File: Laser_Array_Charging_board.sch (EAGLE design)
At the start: 22 parts, among them P1 12V/3V_DC/DC_CONVERTER, X1 6ESRM-P

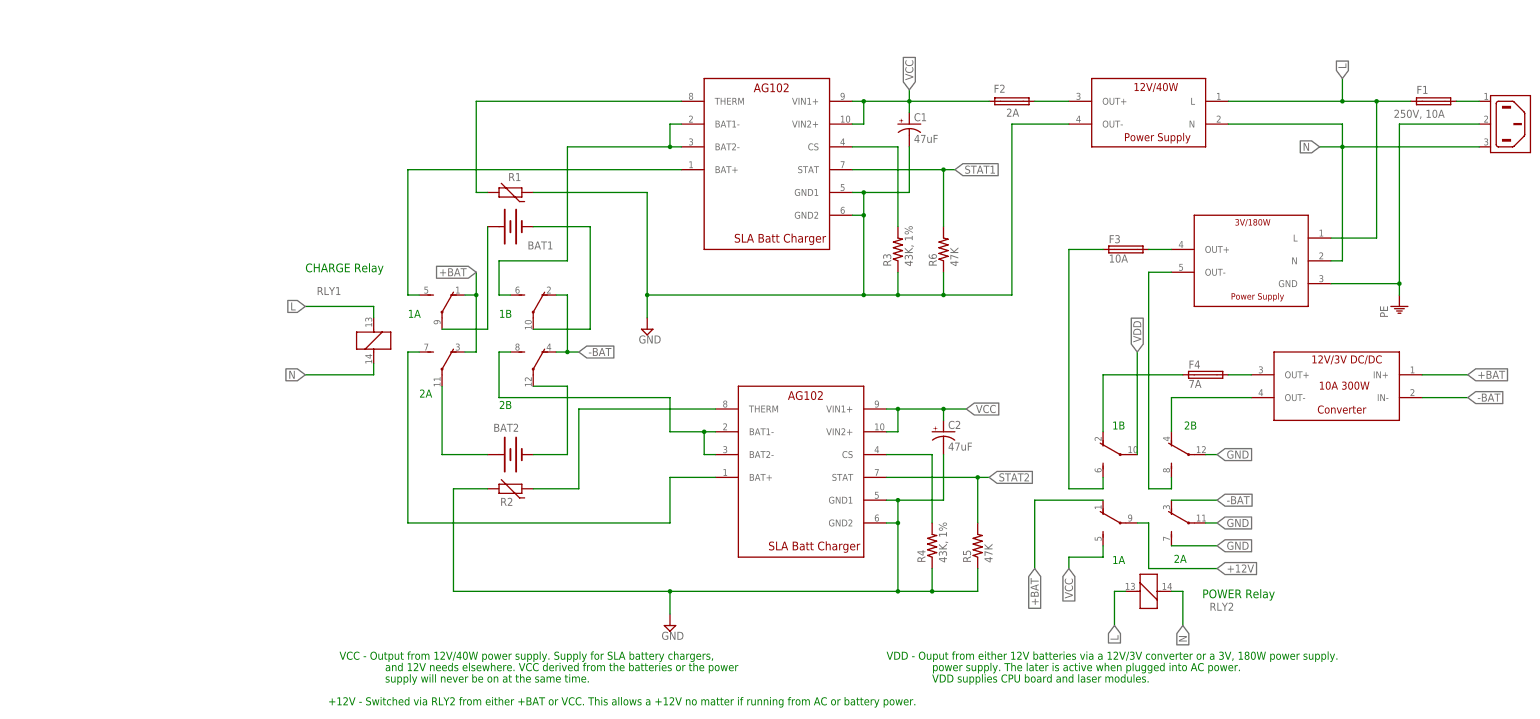
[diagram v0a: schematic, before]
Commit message: CPU board with headers moved over and with programming jack. V1.0
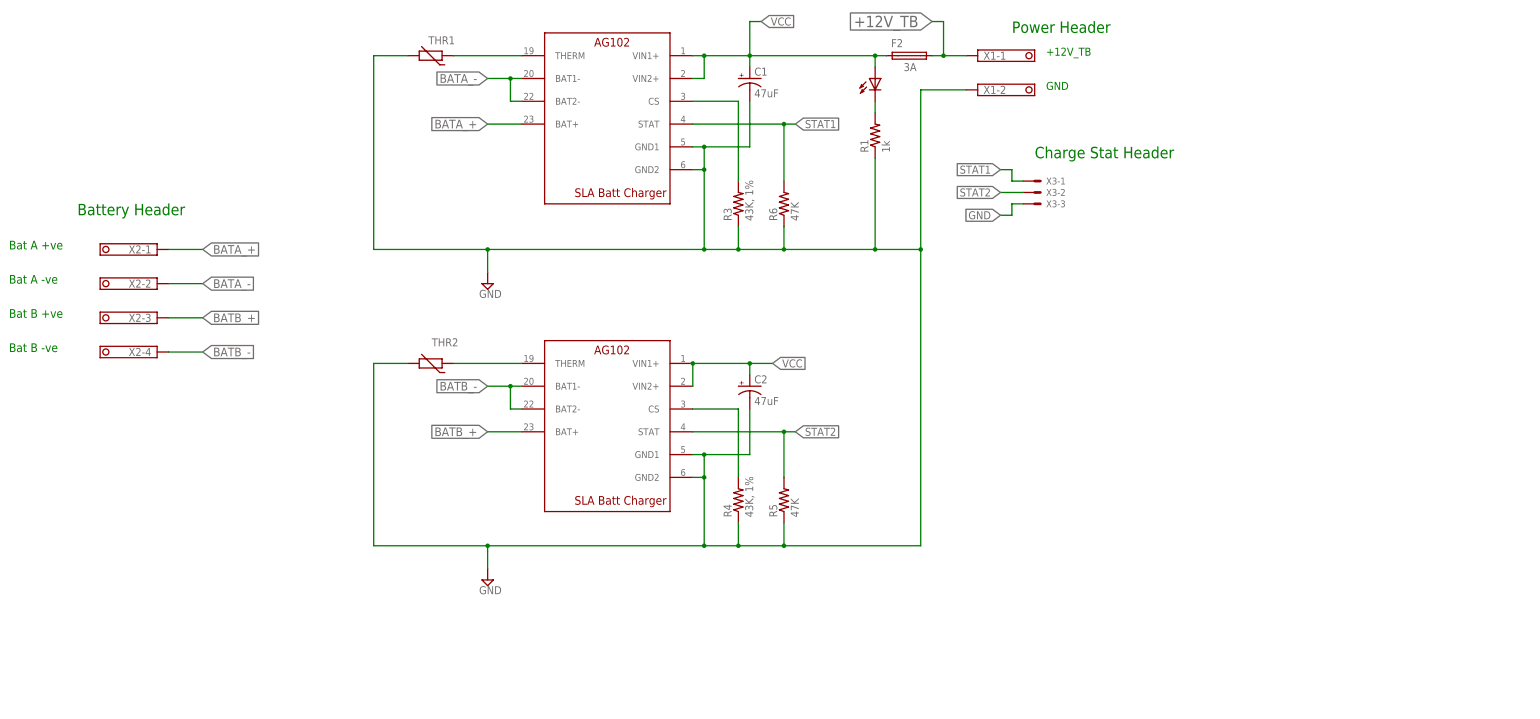
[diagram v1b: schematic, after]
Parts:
- removed BAT1, BAT2: (no value), Mine:BATTERY
- removed F1: 250V, 10A, fuse:SH22,5
- removed F3: 10A, fuse:SH22,5
- removed F4: 7A, fuse:SH22,5
- removed P1: 12V/3V_DC/DC_CONVERTER, Mine:12V/3V_DC/DC_CONVERTER
- removed PS1: 12V/40W_POWER_SUPPLY, Mine:12V/40W_POWER_SUPPLY
- removed PS2: 3V/180W_POWER_SUPPLY, Mine:3V/180W_POWER_SUPPLY
- removed R2: THERMISTOR-2,5, Mine:THERMISTOR-2,5
- removed RLY1, RLY2: 4P4T_RELAYS, Mine:4P4T_RELAYS
- added LED1: LEDCHIPLED_0805, Mine:LEDCHIPLED_0805
- added THR1, THR2: THERMISTOR-2,5, Mine:THERMISTOR-2,5
- added X2: 1751264, con-phoenix-350:1751264
- added X3: 22-23-2031, Mine:22-23-2031
- F2: value 2A -> 3A
- R1: value THERMISTOR-2,5 -> 1k; device Mine:THERMISTOR-2,5 -> rcl:R-US_M0805
- X1: value 6ESRM-P -> 1751248; device con-tycoelectronics:6ESRM-P -> con-phoenix-350:1751248
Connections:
- removed net +12V: RLY21.P
- removed net +BAT: P1.IN+, RLY11.O, RLY13.O, RLY21.O
- removed net -BAT: P1.IN-, RLY12.O, RLY14.O, RLY23.O
- removed net L: F1.1, PS1.L, PS2.L, RLY1_.1, RLY2_.1
- removed net N: PS1.N, PS2.N, RLY1_.2, RLY2_.2, X1.AC2
- removed net N$10: PS2.OUT-, RLY24.S
- removed net N$11: CHG1.BAT+, RLY11.S
- removed net N$12: CHG1.THERM, R1.2
- removed net N$14: CHG2.THERM, R2.1
- removed net N$15: CHG2.BAT1-, CHG2.BAT2-, RLY14.S
- removed net N$16: F1.2, X1.AC1
- removed net N$17: CHG2.BAT+, RLY13.S
- removed net N$18: F2.2, PS1.OUT+
- removed net N$19: F3.2, PS2.OUT+
- removed net N$20: F4.2, P1.OUT+
- removed net N$4: BAT1.-, RLY12.P
- removed net N$5: BAT2.+@1, RLY13.P
- removed net N$6: CHG1.BAT1-, CHG1.BAT2-, RLY12.S
- removed net N$8: BAT2.-, RLY14.P
- removed net N$9: F4.1, RLY22.O
- removed net PE: PS2.GND, X1.SH
- removed net VDD: RLY22.P
- new net +12V_TB: F2.2, X1-1.K
- new net BATA_+: CHG1.BAT+, X2-1.K
- new net BATA_-: CHG1.BAT1-, CHG1.BAT2-, X2-2.K
- new net BATB_+: CHG2.BAT+, X2-3.K
- new net BATB_-: CHG2.BAT1-, CHG2.BAT2-, X2-4.K
- net GND: now also THR1.2, THR2.2, X1-2.K, X3-3.S; no longer PS1.OUT-, R2.2, RLY23.P, RLY23.S, RLY24.P
- net N$1: now also CHG1.THERM, THR1.1; no longer P1.OUT-, RLY24.O
- net N$2: now also CHG2.THERM, THR2.1; no longer F3.1, RLY22.S
- net N$3: now also LED1.C, R1.2; no longer BAT1.+@1, RLY11.P
- net STAT1: now also X3-1.S
- net STAT2: now also X3-2.S
- net VCC: now also LED1.A; no longer RLY21.S
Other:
- note added: "+12V_TB"
- note added: "Bat A +ve"
- note added: "Bat A -ve"
- note added: "Bat B +ve"
- note added: "Bat B -ve"
- note added: "Battery Header"
- note added: "Charge Stat Header"
- note added: "GND"
- note added: "Power Header"
- note removed: "+12V - Switched via RLY2 from either +BAT or VCC. This allows a +12V no matter if running from AC or battery power."
- note removed: "1A"
- note removed: "1B"
- note removed: "2A"
- note removed: "2B"
- note removed: "CHARGE Relay"
- note removed: "POWER Relay"
- note removed: "VCC - Output from 12V/40W power supply. Supply for SLA battery chargers,"
- note removed: "VDD - Ouput from either 12V batteries via a 12V/3V converter or a 3V, 180W power supply."
- note removed: "VDD supplies CPU board and laser modules."
- note removed: "and 12V needs elsewhere. VCC derived from the batteries or the power"
- note removed: "power supply. The later is active when plugged into AC power."
- note removed: "supply will never be on at the same time."
- moved on the sheet: C1, C2, F2, R3, R4, R5, R6

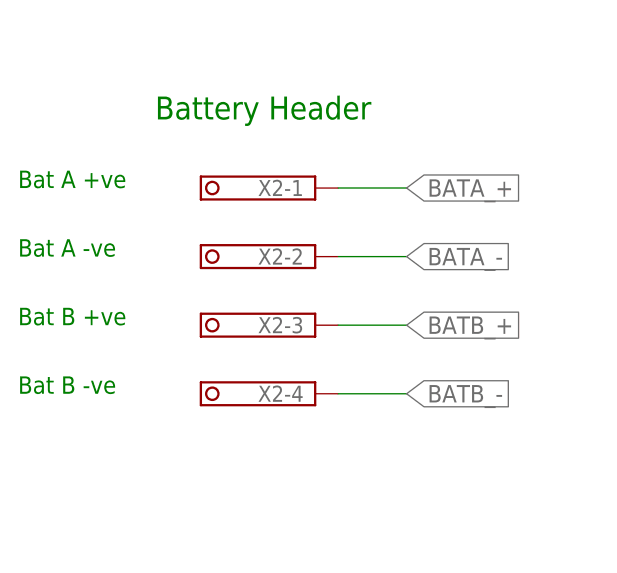
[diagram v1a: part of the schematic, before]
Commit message: Charging Board  header change, V1.1
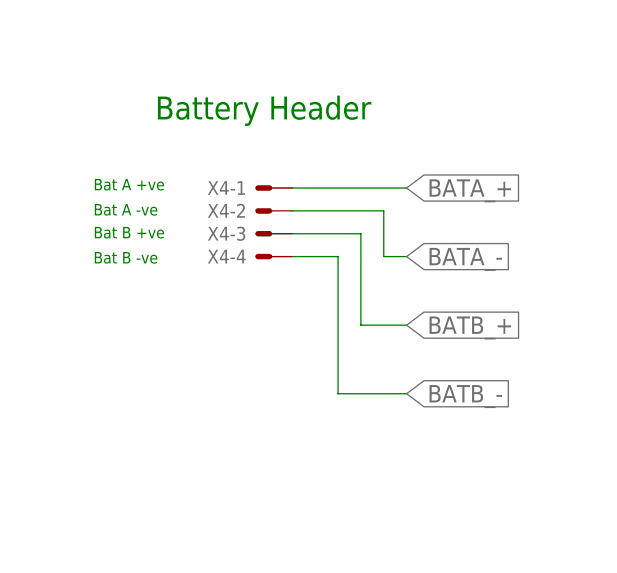
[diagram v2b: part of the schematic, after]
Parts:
- removed X2: 1751264, con-phoenix-350:1751264
- added X4: 22-23-2041, Mine:22-23-2041
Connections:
- net BATA_+: now also X4-1.S; no longer X2-1.K
- net BATA_-: now also X4-2.S; no longer X2-2.K
- net BATB_+: now also X4-3.S; no longer X2-3.K
- net BATB_-: now also X4-4.S; no longer X2-4.K
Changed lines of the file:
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@@
 <part name="F2" library="fuse" deviceset="SH22,5" device="" value="3A"/>
 <part name="CHG2" library="Mine" deviceset="AG102_SLA_CHARGER" device=""/>
-<part name="X2" library="con-phoenix-350" deviceset="1751264" device=""/>
 <part name="X1" library="con-phoenix-350" deviceset="1751248" device=""/>
 <part name="X3" library="Mine" deviceset="22-23-2031" device=""/>
@@
 <part name="LED1" library="Mine" deviceset="LED" device="CHIPLED_0805"/>
 <part name="R1" library="rcl" deviceset="R-US_" device="M0805" value="1k"/>
+<part name="X4" library="Mine" deviceset="22-23-2041" device=""/>
 </parts>
 <sheets>
@@
 <text x="76.2" y="68.58" size="1.778" layer="91">+12V_TB</text>
 <text x="76.2" y="60.96" size="1.778" layer="91">GND</text>
-<text x="-154.94" y="25.4" size="1.9304" layer="91">Bat A +ve</text>
-<text x="-154.94" y="17.78" size="1.9304" layer="91">Bat A -ve</text>
-<text x="-154.94" y="2.54" size="1.9304" layer="91">Bat B -ve</text>
-<text x="-154.94" y="10.16" size="1.9304" layer="91">Bat B +ve</text>
+<text x="-146.558" y="25.146" size="1.27" layer="91">Bat A +ve</text>
+<text x="-146.558" y="22.352" size="1.27" layer="91">Bat A -ve</text>
+<text x="-146.558" y="17.018" size="1.27" layer="91">Bat B -ve</text>
+<text x="-146.558" y="19.812" size="1.27" layer="91">Bat B +ve</text>
 <text x="-139.7" y="33.02" size="2.54" layer="91">Battery Header</text>
 <text x="68.58" y="73.66" size="2.54" layer="91">Power Header</text>
@@
 </instance>
 <instance part="CHG2" gate="G$1" x="-25.4" y="-10.16" rot="MR0"/>
-<instance part="X2" gate="-1" x="-121.92" y="25.4" smashed="yes" rot="MR0">
-<attribute name="NAME" x="-123.19" y="24.511" size="1.778" layer="95" rot="MR0"/>
-</instance>
-<instance part="X2" gate="-2" x="-121.92" y="17.78" smashed="yes" rot="MR0">
-<attribute name="NAME" x="-123.19" y="16.891" size="1.778" layer="95" rot="MR0"/>
-</instance>
-<instance part="X2" gate="-3" x="-121.92" y="10.16" smashed="yes" rot="MR0">
-<attribute name="NAME" x="-123.19" y="9.271" size="1.778" layer="95" rot="MR0"/>
-</instance>
-<instance part="X2" gate="-4" x="-121.92" y="2.54" smashed="yes" rot="MR0">
-<attribute name="NAME" x="-123.19" y="1.651" size="1.778" layer="95" rot="MR0"/>
-</instance>
 <instance part="X1" gate="-1" x="60.96" y="68.58" smashed="yes">
 <attribute name="NAME" x="62.23" y="67.691" size="1.778" layer="95"/>
@@
 <instance part="LED1" gate="G$1" x="38.1" y="63.5"/>
 <instance part="R1" gate="G$1" x="38.1" y="50.8" rot="R90"/>
+<instance part="X4" gate="-1" x="-127" y="25.4" smashed="yes" rot="MR0">
+<attribute name="NAME" x="-129.54" y="24.638" size="1.524" layer="95" rot="MR0"/>
+</instance>
+<instance part="X4" gate="-2" x="-127" y="22.86" smashed="yes" rot="MR0">
+<attribute name="NAME" x="-129.54" y="22.098" size="1.524" layer="95" rot="MR0"/>
+</instance>
+<instance part="X4" gate="-3" x="-127" y="20.32" smashed="yes" rot="MR0">
+<attribute name="NAME" x="-129.54" y="19.558" size="1.524" layer="95" rot="MR0"/>
+</instance>
+<instance part="X4" gate="-4" x="-127" y="17.78" smashed="yes" rot="MR0">
+<attribute name="NAME" x="-129.54" y="17.018" size="1.524" layer="95" rot="MR0"/>
+</instance>
 </instances>
 <busses>
@@
 <net name="BATA_+" class="0">
 <segment>
-<pinref part="X2" gate="-1" pin="K"/>
-<wire x1="-119.38" y1="25.4" x2="-111.76" y2="25.4" width="0.1524" layer="91"/>
+<wire x1="-124.46" y1="25.4" x2="-111.76" y2="25.4" width="0.1524" layer="91"/>
 <label x="-111.76" y="25.4" size="1.9304" layer="95" xref="yes"/>
+<pinref part="X4" gate="-1" pin="S"/>
 </segment>
 <segment>
@@
 </segment>
 <segment>
-<pinref part="X2" gate="-2" pin="K"/>
-<wire x1="-119.38" y1="17.78" x2="-111.76" y2="17.78" width="0.1524" layer="91"/>
 <label x="-111.76" y="17.78" size="1.9304" layer="95" xref="yes"/>
+<pinref part="X4" gate="-2" pin="S"/>
+<wire x1="-114.3" y1="17.78" x2="-111.76" y2="17.78" width="0.1524" layer="91"/>
+<wire x1="-124.46" y1="22.86" x2="-114.3" y2="22.86" width="0.1524" layer="91"/>
+<wire x1="-114.3" y1="22.86" x2="-114.3" y2="17.78" width="0.1524" layer="91"/>
 </segment>
 </net>
@@
 </segment>
 <segment>
-<pinref part="X2" gate="-3" pin="K"/>
-<wire x1="-119.38" y1="10.16" x2="-111.76" y2="10.16" width="0.1524" layer="91"/>
 <label x="-111.76" y="10.16" size="1.9304" layer="95" xref="yes"/>
+<pinref part="X4" gate="-3" pin="S"/>
+<wire x1="-124.46" y1="20.32" x2="-116.84" y2="20.32" width="0.1524" layer="91"/>
+<wire x1="-116.84" y1="20.32" x2="-116.84" y2="10.16" width="0.1524" layer="91"/>
+<wire x1="-116.84" y1="10.16" x2="-111.76" y2="10.16" width="0.1524" layer="91"/>
 </segment>
 </net>
 <net name="BATB_-" class="0">
 <segment>
-<pinref part="X2" gate="-4" pin="K"/>
 <wire x1="-119.38" y1="2.54" x2="-111.76" y2="2.54" width="0.1524" layer="91"/>
 <label x="-111.76" y="2.54" size="1.9304" layer="95" xref="yes"/>
-</segment>
-<segment>
+<pinref part="X4" gate="-4" pin="S"/>
+<wire x1="-124.46" y1="17.78" x2="-119.38" y2="17.78" width="0.1524" layer="91"/>
+<wire x1="-119.38" y1="17.78" x2="-119.38" y2="2.54" width="0.1524" layer="91"/>
+</segment>
+<segment>

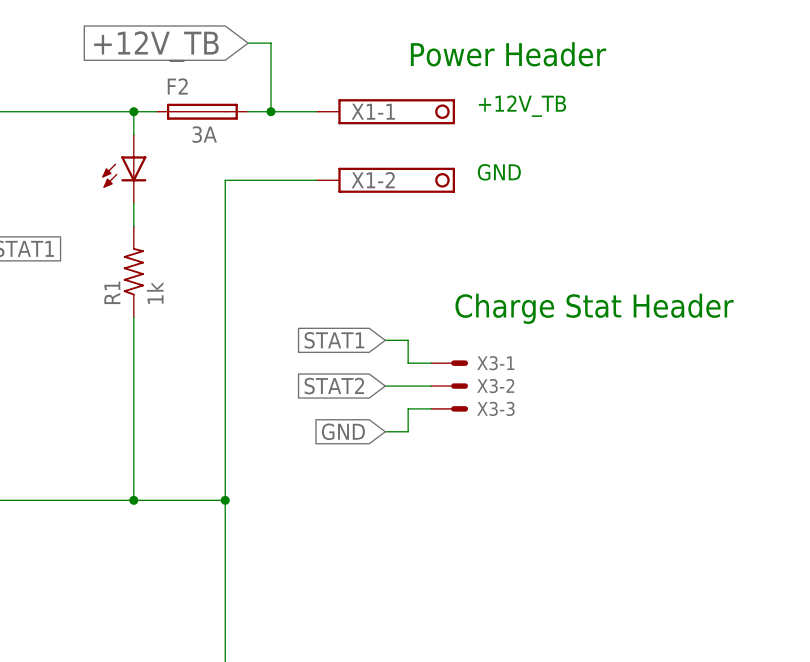
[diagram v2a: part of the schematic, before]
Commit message: Charging Board  header change, V1.1, again
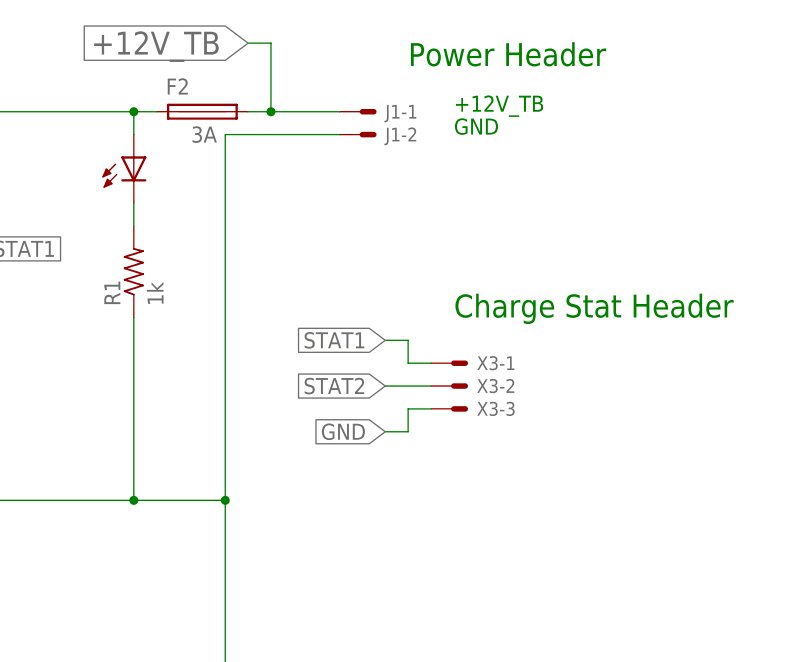
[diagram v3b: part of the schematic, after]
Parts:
- removed X1: 1751248, con-phoenix-350:1751248
- added J1: 22-23-2021, Mine:22-23-2021
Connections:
- net +12V_TB: now also J1-1.S; no longer X1-1.K
- net GND: now also J1-2.S; no longer X1-2.K
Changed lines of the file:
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@@
 <part name="F2" library="fuse" deviceset="SH22,5" device="" value="3A"/>
 <part name="CHG2" library="Mine" deviceset="AG102_SLA_CHARGER" device=""/>
-<part name="X1" library="con-phoenix-350" deviceset="1751248" device=""/>
 <part name="X3" library="Mine" deviceset="22-23-2031" device=""/>
 <part name="CHG1" library="Mine" deviceset="AG102_SLA_CHARGER" device=""/>
@@
 <part name="R1" library="rcl" deviceset="R-US_" device="M0805" value="1k"/>
 <part name="X4" library="Mine" deviceset="22-23-2041" device=""/>
+<part name="J1" library="Mine" deviceset="22-23-2021" device=""/>
 </parts>
 <sheets>
 <sheet>
 <plain>
-<text x="76.2" y="68.58" size="1.778" layer="91">+12V_TB</text>
-<text x="76.2" y="60.96" size="1.778" layer="91">GND</text>
+<text x="73.66" y="68.58" size="1.778" layer="91">+12V_TB</text>
+<text x="73.66" y="66.04" size="1.778" layer="91">GND</text>
 <text x="-146.558" y="25.146" size="1.27" layer="91">Bat A +ve</text>
 <text x="-146.558" y="22.352" size="1.27" layer="91">Bat A -ve</text>
@@
 </instance>
 <instance part="CHG2" gate="G$1" x="-25.4" y="-10.16" rot="MR0"/>
-<instance part="X1" gate="-1" x="60.96" y="68.58" smashed="yes">
-<attribute name="NAME" x="62.23" y="67.691" size="1.778" layer="95"/>
-</instance>
-<instance part="X1" gate="-2" x="60.96" y="60.96" smashed="yes">
-<attribute name="NAME" x="62.23" y="60.071" size="1.778" layer="95"/>
-</instance>
 <instance part="X3" gate="-1" x="73.66" y="40.64" smashed="yes">
 <attribute name="NAME" x="76.2" y="39.878" size="1.524" layer="95"/>
@@
 <instance part="X4" gate="-4" x="-127" y="17.78" smashed="yes" rot="MR0">
 <attribute name="NAME" x="-129.54" y="17.018" size="1.524" layer="95" rot="MR0"/>
+</instance>
+<instance part="J1" gate="-1" x="63.5" y="68.58" smashed="yes">
+<attribute name="NAME" x="66.04" y="67.818" size="1.524" layer="95"/>
+</instance>
+<instance part="J1" gate="-2" x="63.5" y="66.04" smashed="yes">
+<attribute name="NAME" x="66.04" y="65.278" size="1.524" layer="95"/>
 </instance>
 </instances>
@@
 <pinref part="THR1" gate="G$1" pin="2"/>
 <wire x1="-66.04" y1="68.58" x2="-73.66" y2="68.58" width="0.1524" layer="91"/>
-<pinref part="X1" gate="-2" pin="K"/>
-<wire x1="58.42" y1="60.96" x2="48.26" y2="60.96" width="0.1524" layer="91"/>
 <pinref part="THR2" gate="G$1" pin="2"/>
 <wire x1="-66.04" y1="0" x2="-73.66" y2="0" width="0.1524" layer="91"/>
@@
 <wire x1="7.62" y1="-40.64" x2="0" y2="-40.64" width="0.1524" layer="91"/>
 <wire x1="0" y1="-40.64" x2="-48.26" y2="-40.64" width="0.1524" layer="91"/>
-<wire x1="48.26" y1="60.96" x2="48.26" y2="25.4" width="0.1524" layer="91"/>
+<wire x1="48.26" y1="66.04" x2="48.26" y2="25.4" width="0.1524" layer="91"/>
 <wire x1="48.26" y1="25.4" x2="48.26" y2="-40.64" width="0.1524" layer="91"/>
 <wire x1="48.26" y1="-40.64" x2="17.78" y2="-40.64" width="0.1524" layer="91"/>
@@
 <wire x1="38.1" y1="45.72" x2="38.1" y2="25.4" width="0.1524" layer="91"/>
 <junction x="38.1" y="25.4"/>
+<pinref part="J1" gate="-2" pin="S"/>
+<wire x1="60.96" y1="66.04" x2="48.26" y2="66.04" width="0.1524" layer="91"/>
 </segment>
 <segment>
@@
 <net name="+12V_TB" class="0">
 <segment>
-<pinref part="X1" gate="-1" pin="K"/>
 <pinref part="F2" gate="1" pin="2"/>
-<wire x1="58.42" y1="68.58" x2="53.34" y2="68.58" width="0.1524" layer="91"/>
+<wire x1="60.96" y1="68.58" x2="53.34" y2="68.58" width="0.1524" layer="91"/>
 <wire x1="53.34" y1="68.58" x2="50.8" y2="68.58" width="0.1524" layer="91"/>
 <wire x1="53.34" y1="68.58" x2="53.34" y2="76.2" width="0.1524" layer="91"/>
@@
 <wire x1="53.34" y1="76.2" x2="50.8" y2="76.2" width="0.1524" layer="91"/>
 <label x="50.8" y="76.2" size="2.54" layer="95" rot="R180" xref="yes"/>
-</segment>
-</net>
+<pinref part="J1" gate="-1" pin="S"/>
+</segment>
+</net>
